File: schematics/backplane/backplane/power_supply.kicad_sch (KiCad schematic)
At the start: 52 parts, among them IC1 LM61480Q5RPHRQ1, IC2 TPS563201DDCR, J2 24v, Q10 SQJ433EP, Q14 NX138BKMYL, Q15 NX138BKMYL, Q16 SQJ433EP, Q17 SQJ433EP, Q9 NX138BKMYL, U2 INA228, U3 INA228, U4 INA228

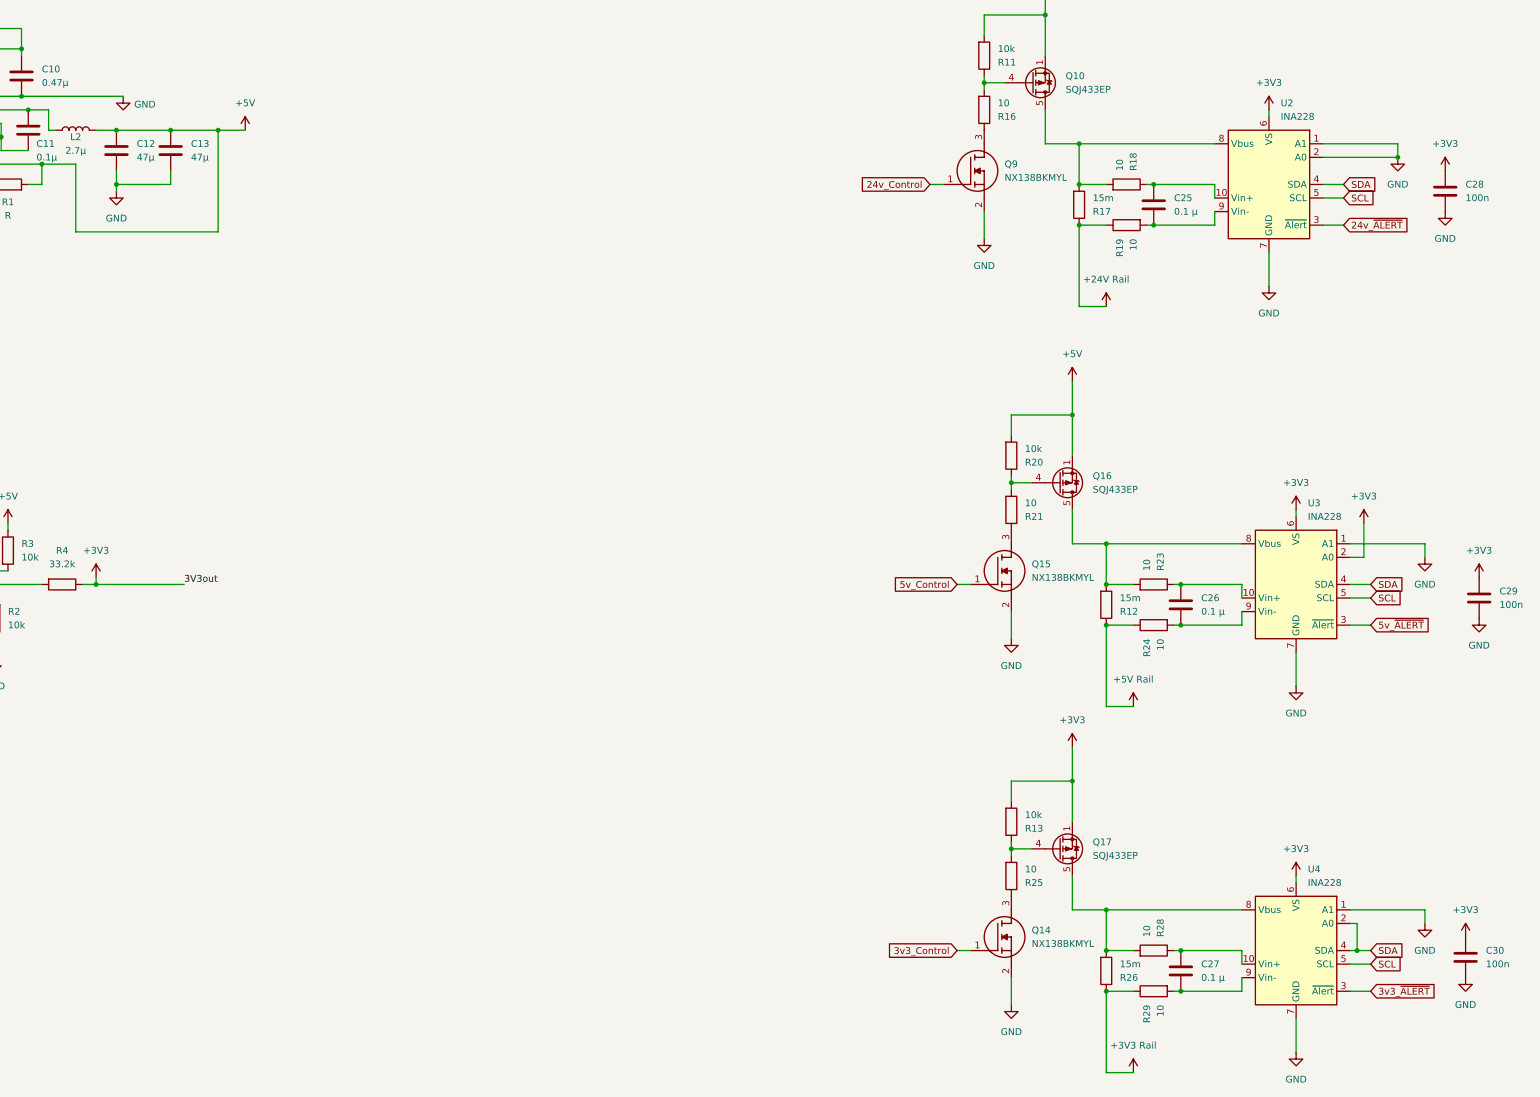
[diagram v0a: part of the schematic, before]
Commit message: Add crystal data and Test points
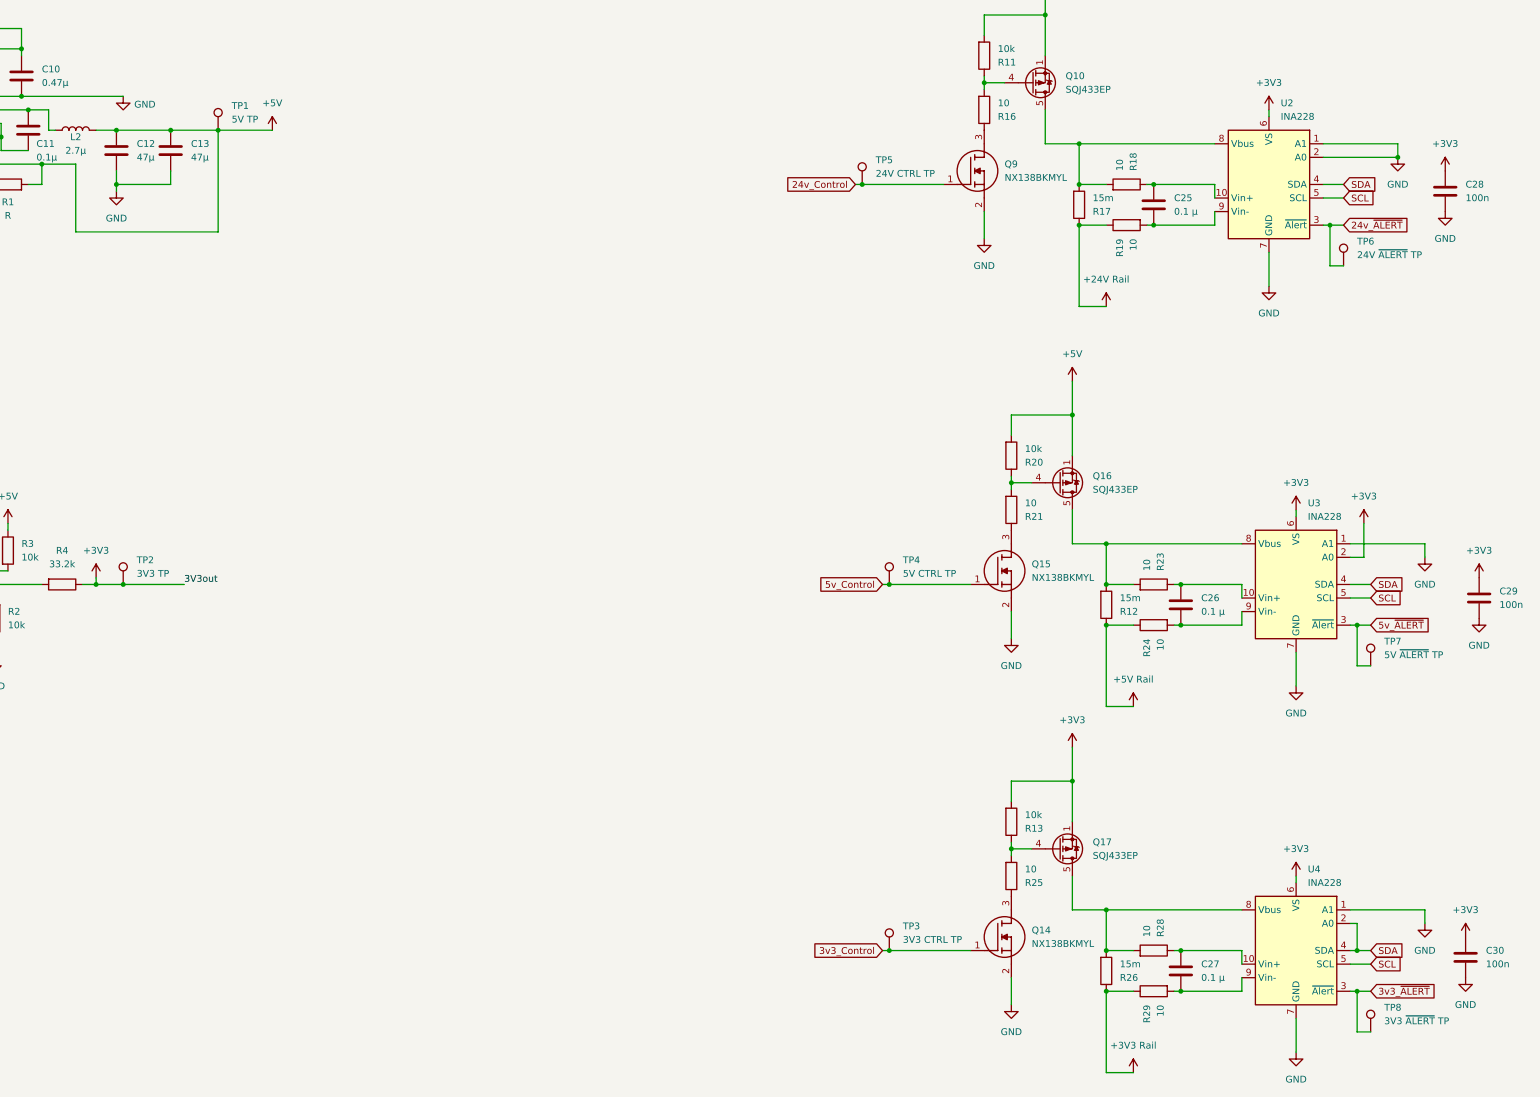
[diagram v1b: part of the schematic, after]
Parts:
- added TP1: 5V TP, TestPoint:TestPoint_Keystone_5000-5004_Miniature, symbol Connector:TestPoint
- added TP2: 3V3 TP, TestPoint:TestPoint_Keystone_5000-5004_Miniature, symbol Connector:TestPoint
- added TP3: 3V3 CTRL TP, TestPoint:TestPoint_Keystone_5000-5004_Miniature, symbol Connector:TestPoint
- added TP4: 5V CTRL TP, TestPoint:TestPoint_Keystone_5000-5004_Miniature, symbol Connector:TestPoint
- added TP5: 24V CTRL TP, TestPoint:TestPoint_Keystone_5000-5004_Miniature, symbol Connector:TestPoint
- added TP6: 24V ~{ALERT} TP, TestPoint:TestPoint_Keystone_5000-5004_Miniature, symbol Connector:TestPoint
- added TP7: 5V ~{ALERT} TP, TestPoint:TestPoint_Keystone_5000-5004_Miniature, symbol Connector:TestPoint
- added TP8: 3V3 ~{ALERT} TP, TestPoint:TestPoint_Keystone_5000-5004_Miniature, symbol Connector:TestPoint
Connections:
- net +3V3: now also TP2.1
- net +5V: now also TP1.1
- net 24v_Control: now also TP5.1
- net 24v_~{ALERT}: now also TP6.1
- net 3v3_Control: now also TP3.1
- net 3v3_~{ALERT}: now also TP8.1
- net 5v_Control: now also TP4.1
- net 5v_~{ALERT}: now also TP7.1
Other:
- title: (none) -> Power supply and control

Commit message: redo numbering
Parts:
- renumbered C1 to C13, C4 to C14, C10 to C15, C11 to C16, C12 to C17, C13 to C18, C6 to C19, C9 to C20, C2 to C21, C5 to C22, C3 to C23, C7 to C24, C8 to C25, C28 to C26, C25 to C27, C29 to C28, C26 to C29, C27 to C31, IC1 to IC2, IC2 to IC3, J2 to J13, L2 to L1, L1 to L2, Q10 to Q1, Q9 to Q2, Q16 to Q3, Q15 to Q4, Q17 to Q5, Q14 to Q6, R19 to R10, R20 to R11, R21 to R12, R23 to R13, R12 to R14, R24 to R15, R13 to R16, R25 to R17, R28 to R18, R26 to R19, R1 to R2, R29 to R20, R2 to R5, R11 to R6, R16 to R7, R18 to R8, R17 to R9, TP8 to TP10, TP1 to TP3, TP2 to TP4, TP4 to TP7, TP7 to TP8, TP3 to TP9
